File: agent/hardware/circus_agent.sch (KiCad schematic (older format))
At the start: 53 parts

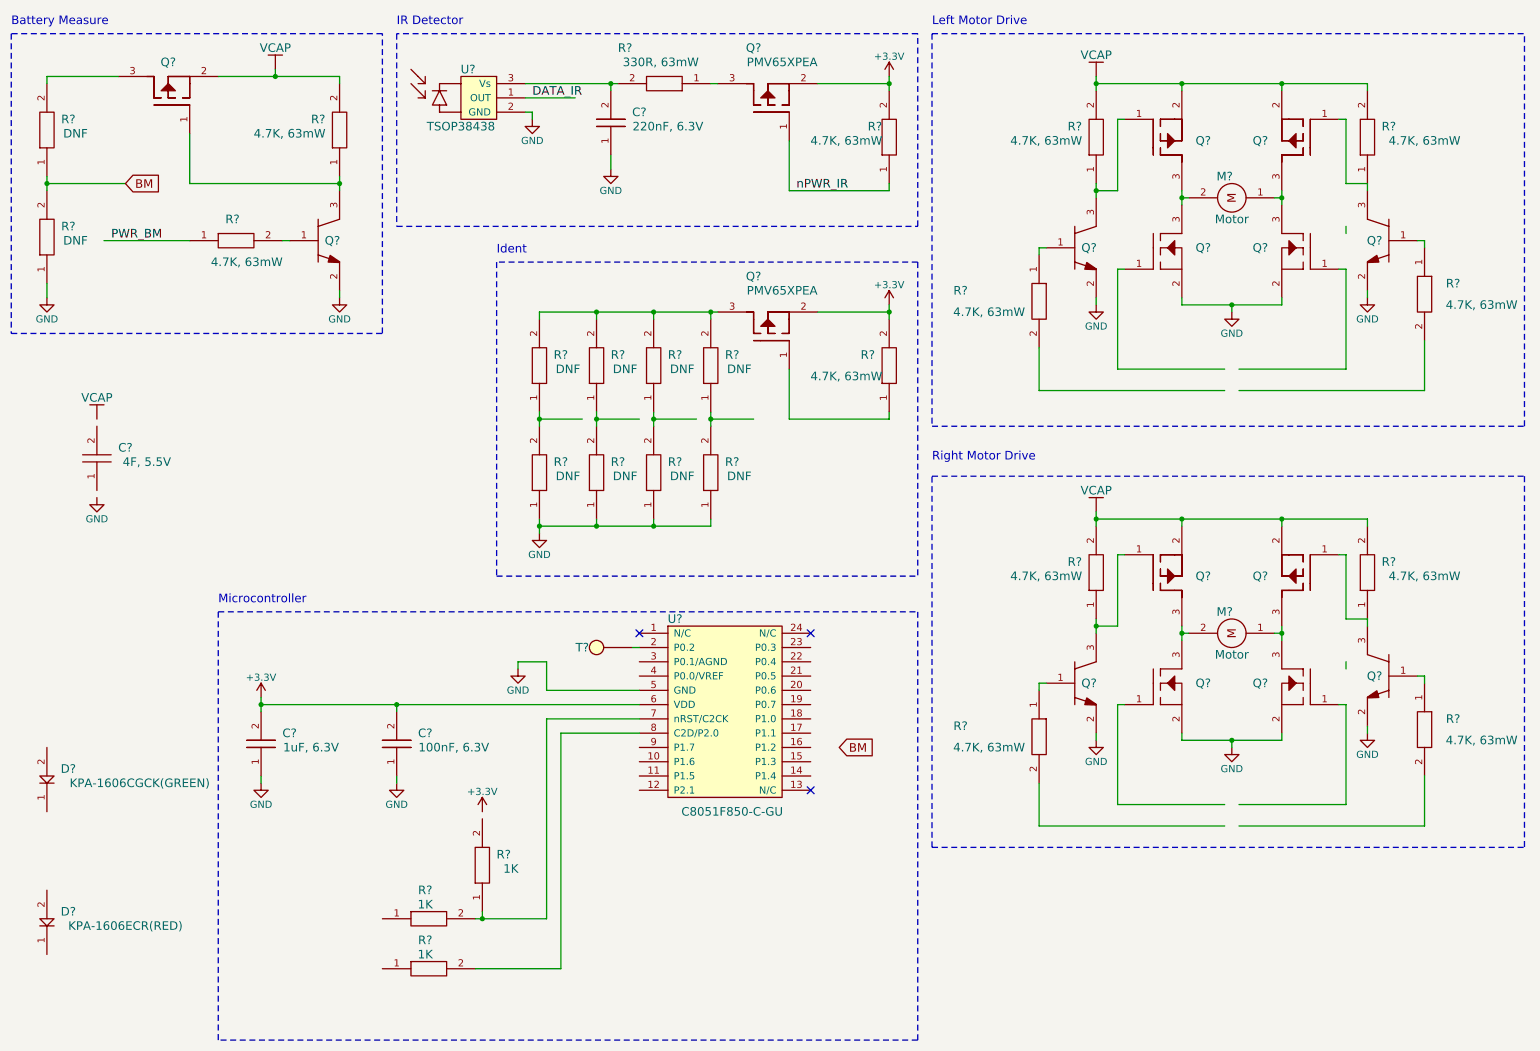
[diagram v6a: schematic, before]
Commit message: added the pinout, LDO
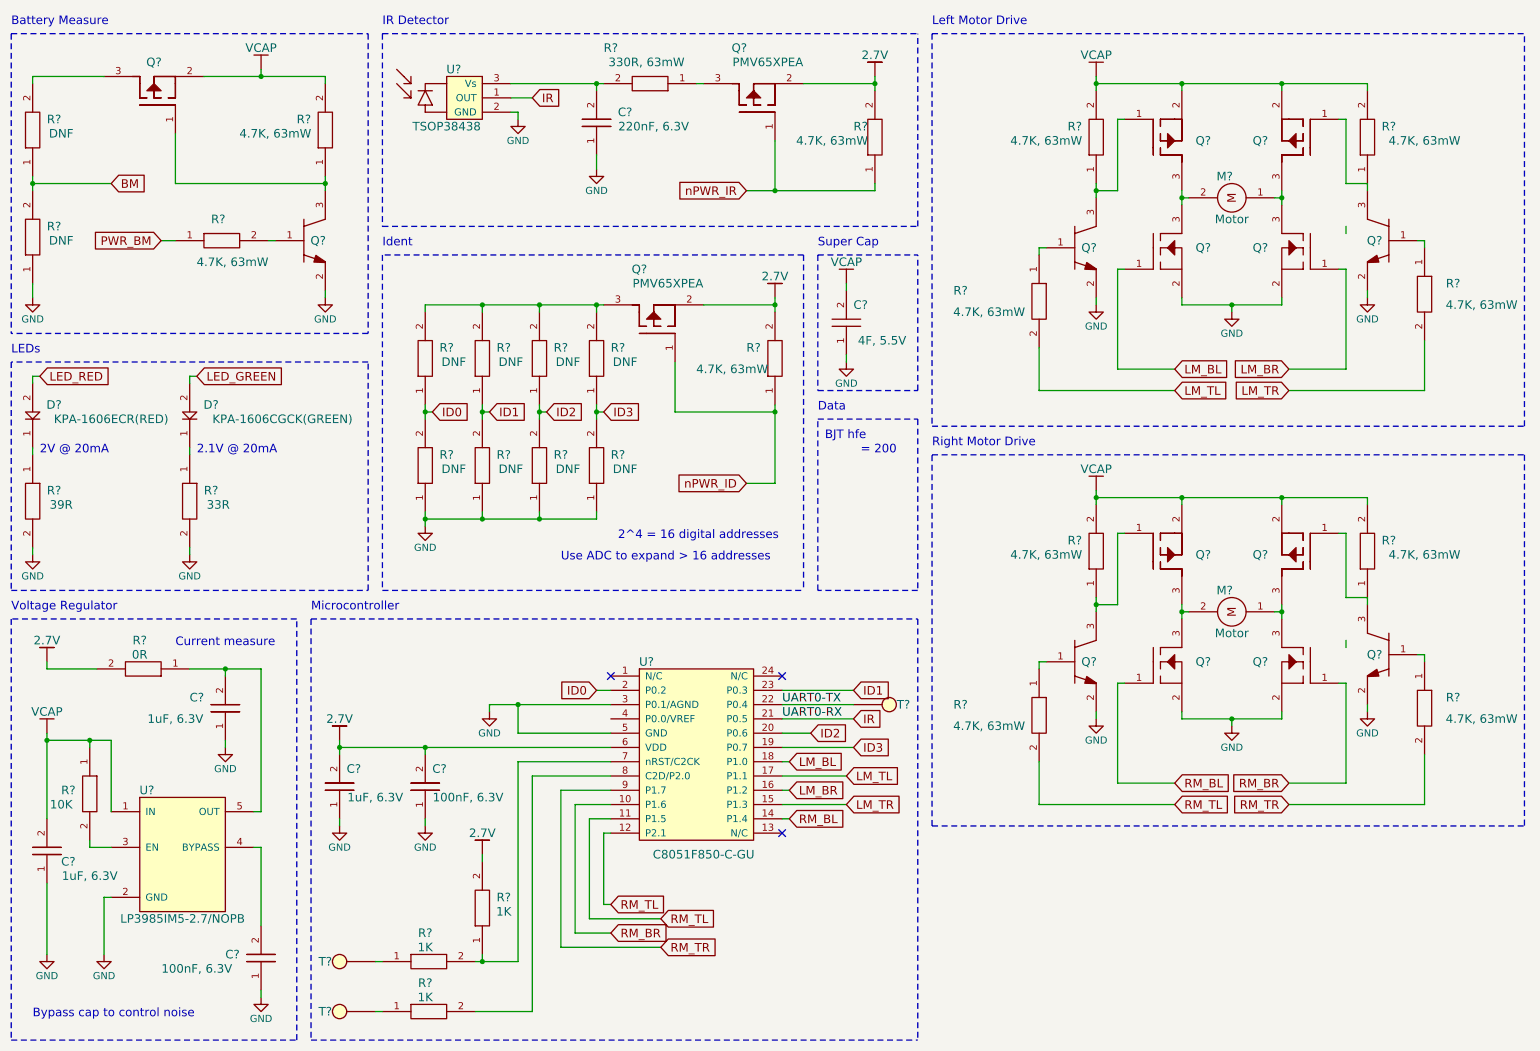
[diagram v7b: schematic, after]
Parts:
- removed T?: TestPoint, symbol TestPoint
- added C? (x2): 1uF, 6.3V, symbol MC0402X224K6R3CT
- added C?: 100nF, 6.3V, symbol MC0402X224K6R3CT
- added R?: 39R, symbol CRCW0402330RFKED
- added R?: 33R, symbol CRCW0402330RFKED
- added R?: 10K, symbol CRCW0402330RFKED
- added R?: 0R, symbol CRCW0402330RFKED
- added T? (x3): TestPoint, symbol TestPoint
- added U?: LP3985IM5-2.7/NOPB, symbol LP3985
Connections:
- net labels added: 2.7V, ID0, ID1, ID2, ID3, IR, LED_GREEN, LED_RED, LM_BL, LM_BR, LM_TL, LM_TR, RM_BL, RM_BR, RM_TL, RM_TR, UART0-RX, UART0-TX, nPWR_ID
- net labels removed: +3.3V, DATA_IR
- wire segments 142 -> 197
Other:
- note added: "2.1V @ 20mA"
- note added: "2V @ 20mA"
- note added: "2^4 = 16 digital addresses"
- note added: "= 200"
- note added: "BJT hfe"
- note added: "Bypass cap to control noise"
- note added: "Current measure"
- note added: "Data"
- note added: "LEDs\n"
- note added: "Super Cap"
- note added: "Use ADC to expand > 16 addresses"
- note added: "Voltage Regulator"
- moved on the sheet: C?, D?, M?, Q?, R?, U?

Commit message: Duel drive with LEDs and ID. Added header
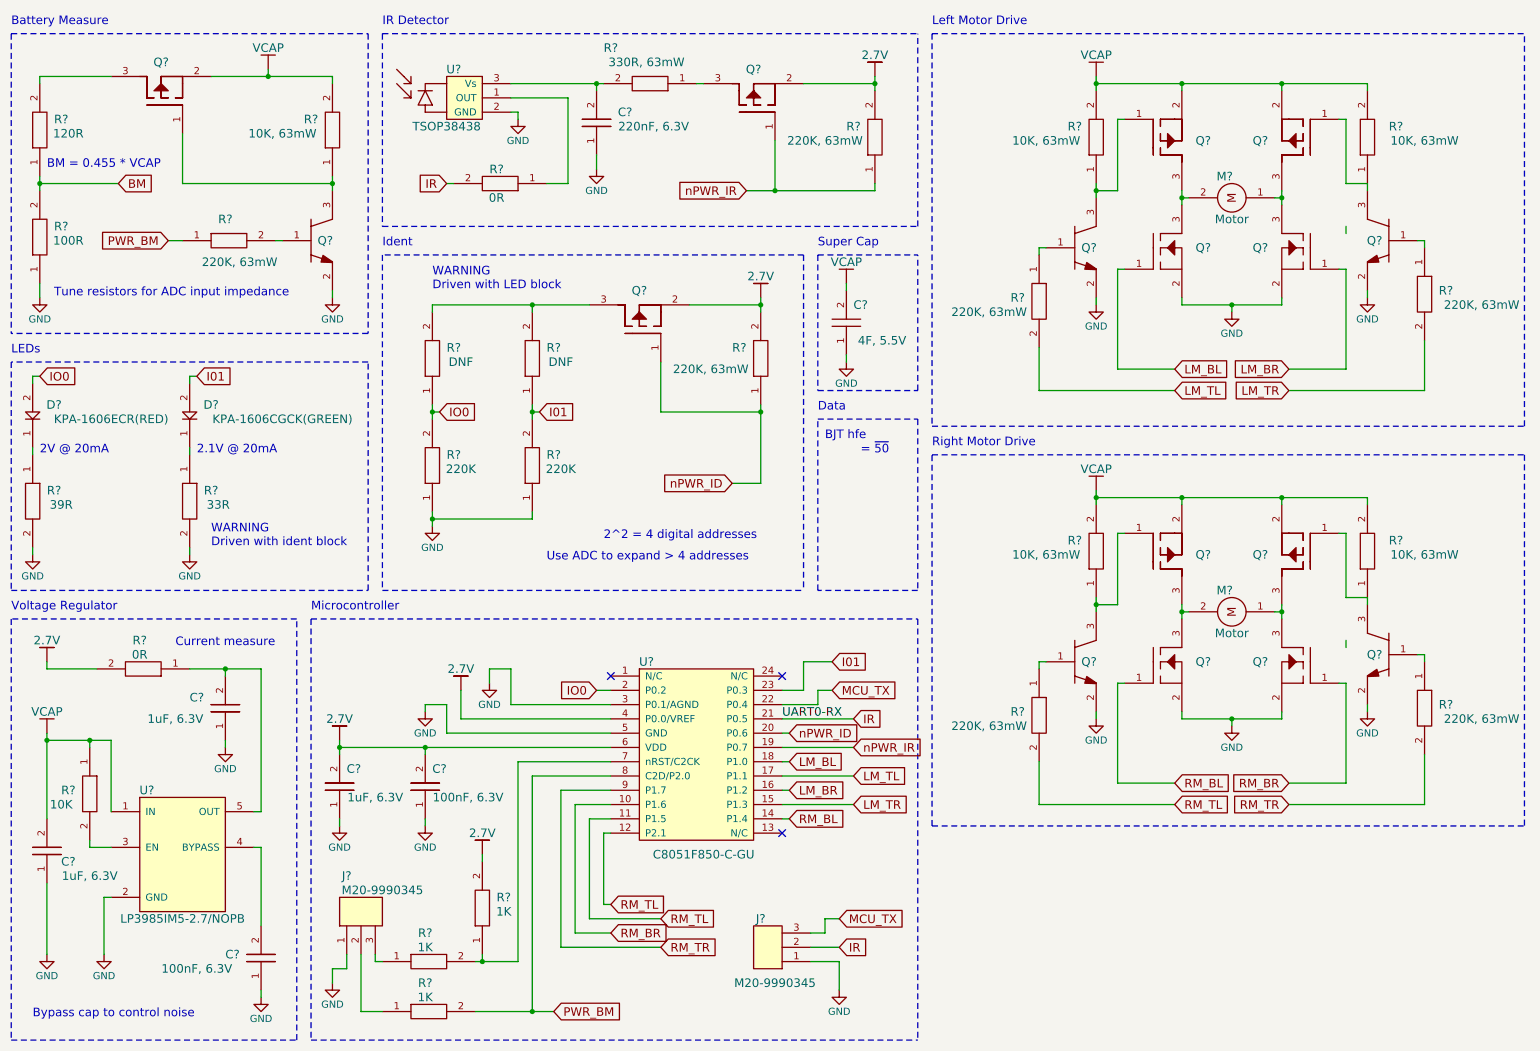
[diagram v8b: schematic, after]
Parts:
- removed R? (x4): DNF, symbol CRCW0402330RFKED
- removed T? (x3): TestPoint, symbol TestPoint
- removed U?: C8051F850-C-GU, symbol C8051F850-C-GU
- added J? (x2): M20-9990345, symbol M20-9990345
- added R?: 0R, symbol CRCW0402330RFKED
- added U?: C8051F850-C-GU, symbol C8051F850-C-GU
- R? (x7): value 4.7K, 63mW -> 220K, 63mW
- R? (x5): value 4.7K, 63mW -> 10K, 63mW
- R? (x2): value DNF -> 220K
- R?: value DNF -> 120R
- R?: value DNF -> 100R
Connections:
- net LED_GREEN is gone; now on net I01: D?.2
- net LED_RED is gone; now on net IO0: D?.2
- net GND: now also J?.1, J?.1, U?.3 (P0.1/AGND), U?.5 (GND)
- net IR: now also J?.2, R?.2, U?.21 (P0.5); no longer U?.1 (OUT)
- net LM_BL: now also U?.18 (P1.0)
- net LM_BR: now also U?.16 (P1.2)
- net LM_TL: now also U?.17 (P1.1)
- net LM_TR: now also U?.15 (P1.3)
- net PWR_BM: now also R?.2, U?.8 (C2D/P2.0)
- net RM_BL: now also U?.14 (P1.4)
- net RM_BR: now also U?.10 (P1.6)
- net RM_TL: now also U?.11 (P1.5), U?.12 (P2.1)
- net RM_TR: now also U?.9 (P1.7)
- net nPWR_ID: now also U?.20 (P0.6)
- net nPWR_IR: now also U?.19 (P0.7)
- net at C?.2, C?.2: now also U?.6 (VDD)
- net at R?.1, R?.2: now also U?.7 (nRST/C2CK)
- net at R?.1: now also J?.3
- net at R?.1: now also J?.2
- net ID0 renamed IO0
- net IO0: now also U?.2 (P0.2)
- net ID1 renamed I01
- net I01: now also U?.23 (P0.3)
- new net: R?.1, U?.1 (OUT)
- new net MCU_TX: J?.3, U?.22 (P0.4)
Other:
- note added: "2^2 = 4 digital addresses"
- note added: "= ~50"
- note added: "BM = 0.455 * VCAP"
- note added: "Tune resistors for ADC input impedance"
- note added: "Use ADC to expand > 4 addresses"
- note added: "WARNING\nDriven with LED block"
- note added: "WARNING\nDriven with ident block"
- note removed: "2^4 = 16 digital addresses"
- note removed: "= 200"
- note removed: "Use ADC to expand > 16 addresses"
- moved on the sheet: Q?, R?
